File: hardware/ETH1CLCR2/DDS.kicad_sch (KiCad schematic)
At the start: 105 parts, among them Q1201 FDV301N, Q1202 2SC3326B, Q1203 DTA144E, Q1204 DTC114E, U1201 LMH6639MA, U1202 AD9834, U1203 AD8038ARZ, U1204 DAC7811, U1205 AD8038ARZ, U1206 DG409DY, U1207 LMH6639MA, U1208 TL431DBZ, U1209 SN74LVC1T45DBV, U1210 SN74LVC1T45DBV, U1211 74AHC1G14, U1212 SN74LVC1T45DBV, U1213 74AUP1G79, U1214 74AC161, U1215 74AC161, U1216 SN74LVC1T45DBV, X1201 830208220601

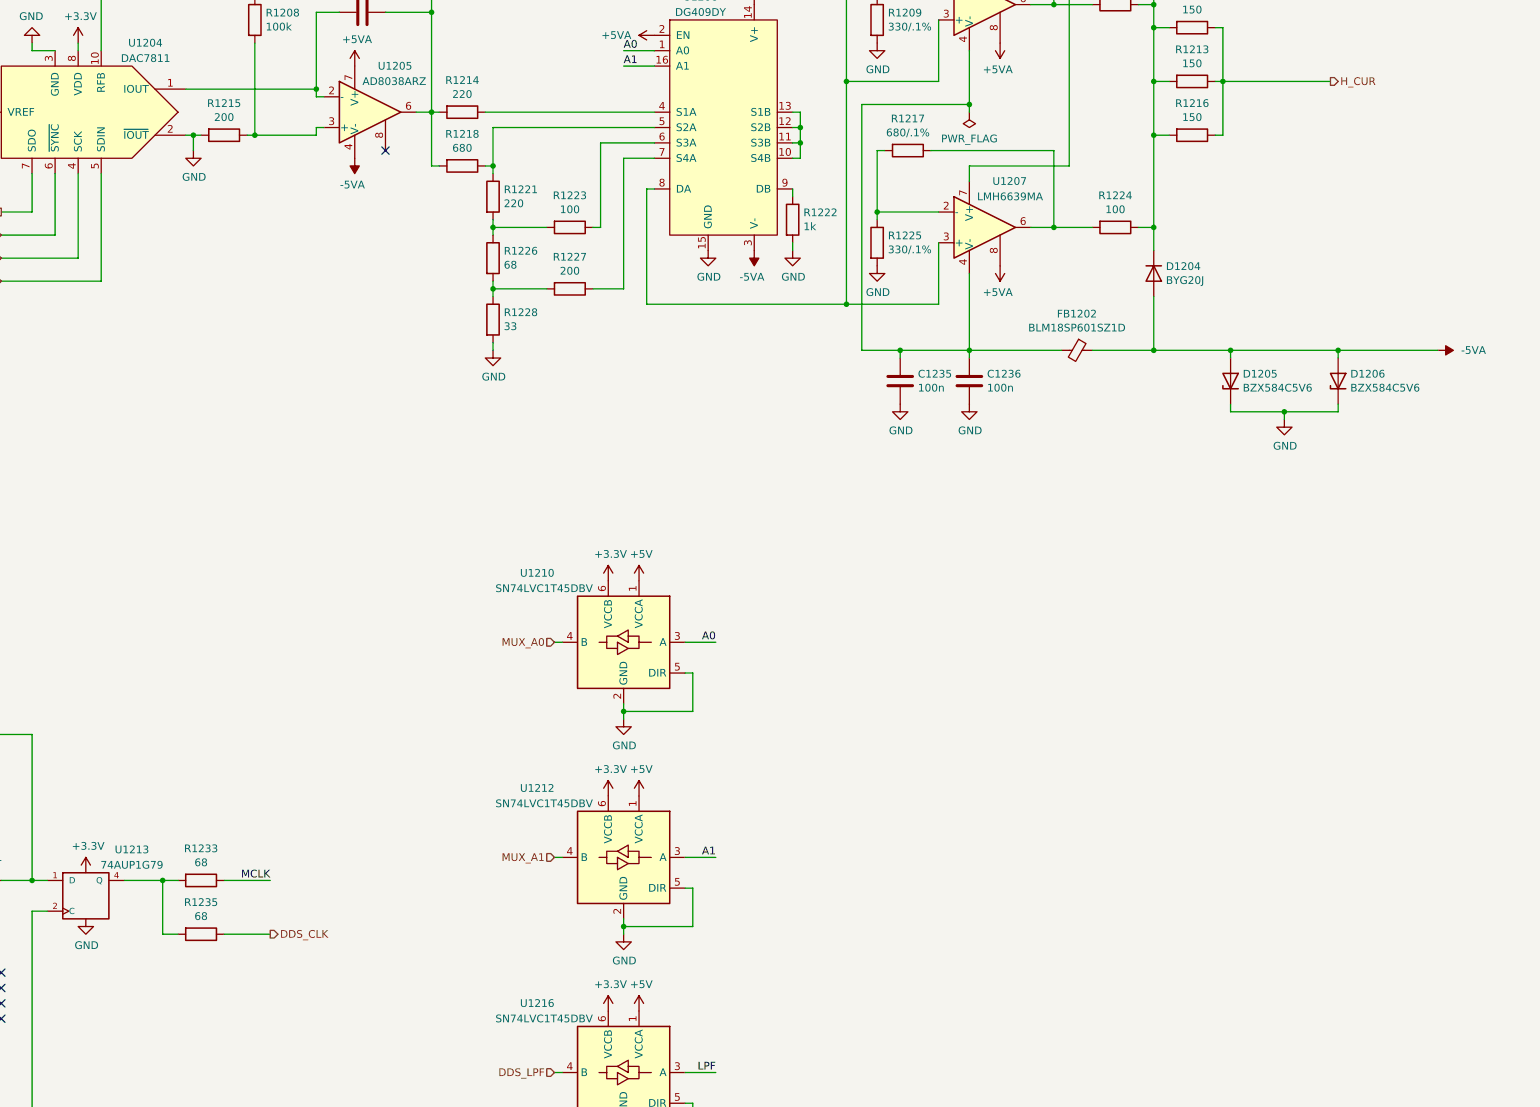
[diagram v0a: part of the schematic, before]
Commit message: Added text to schematics, software development.
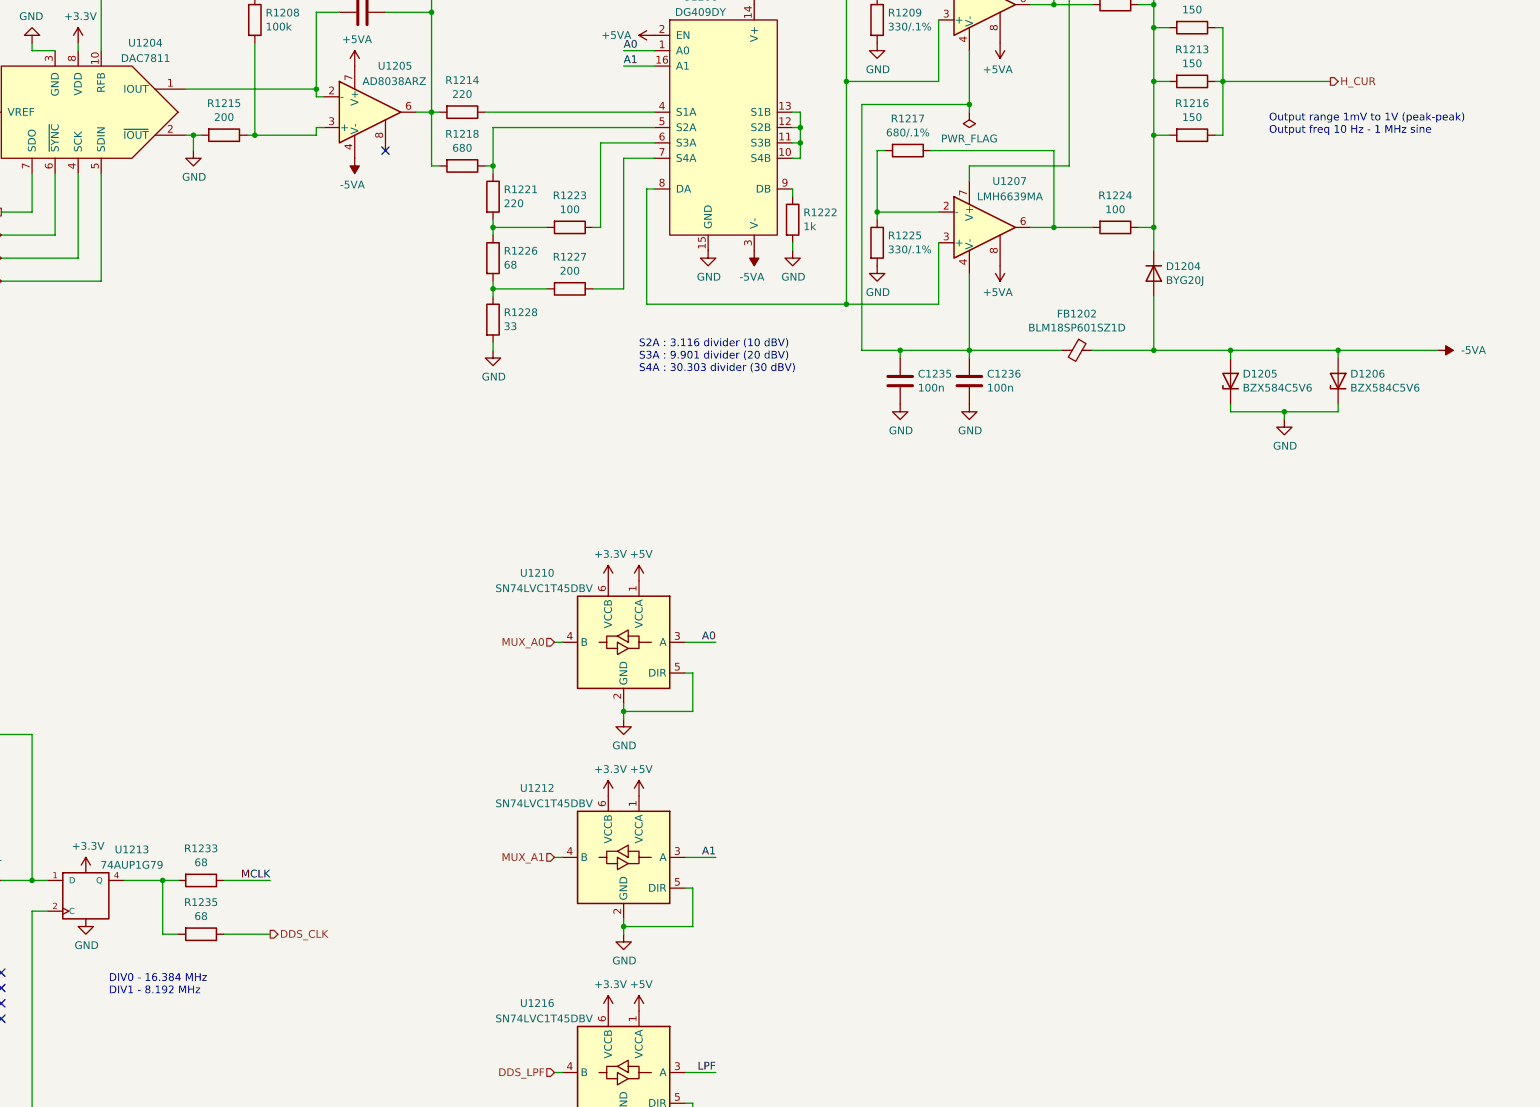
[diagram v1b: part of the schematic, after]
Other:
- note added: "DIV0 - 16.384 MHz DIV1 - 8.192 MHz"
- note added: "Output range 1mV to 1V (peak-peak) Output freq 10 Hz - 1 MHz sine"
- note added: "S2A : 3.116 divider (10 dBV) S3A : 9.901 divider (20 dBV) S4A : 30.303 divider (30 dBV)"
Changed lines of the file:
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@@
     (stroke (width 0) (type default) (color 0 0 0 0))
+  )
+  (text "Output range 1mV to 1V (peak-peak)\nOutput freq 10 Hz - 1 MHz sine"
+    (at 365.76 76.2 0)
+    (effects (font (size 1.27 1.27)) (justify left bottom))
+  )
+  (text "S2A : 3.116 divider (10 dBV)\nS3A : 9.901 divider (20 dBV)\nS4A : 30.303 divider (30 dBV)"
+    (at 261.62 115.57 0)
+    (effects (font (size 1.27 1.27)) (justify left bottom))
+  )
+  (text "DIV0 - 16.384 MHz\nDIV1 - 8.192 MHz" (at 173.99 218.44 0)
+    (effects (font (size 1.27 1.27)) (justify left bottom))
   )
   (label "A0" (at 259.08 62.23 0)

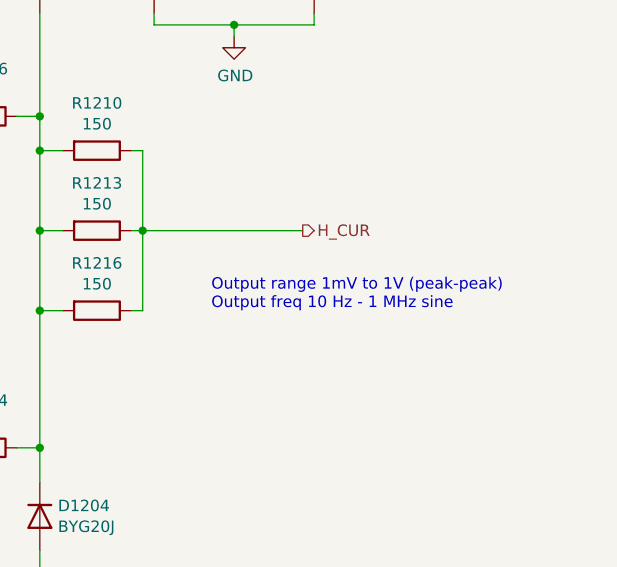
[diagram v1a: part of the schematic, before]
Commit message: Software development and added comments to the schematics.
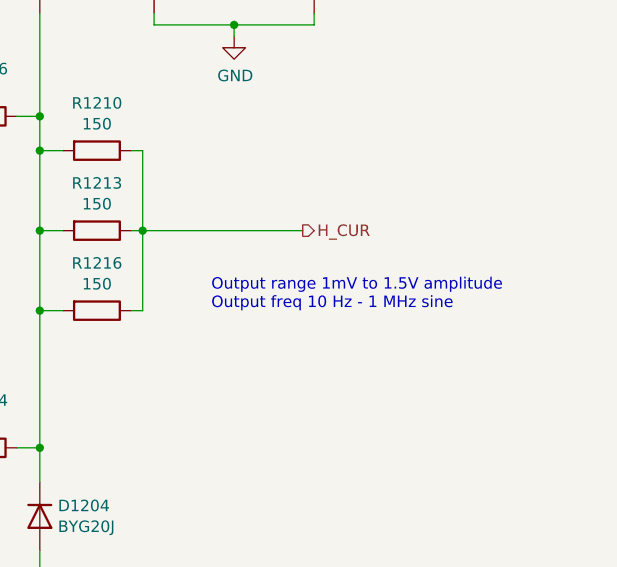
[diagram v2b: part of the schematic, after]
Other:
- note added: "Output range 1mV to 1.5V amplitude Output freq 10 Hz - 1 MHz sine"
- note removed: "Output range 1mV to 1V (peak-peak) Output freq 10 Hz - 1 MHz sine"
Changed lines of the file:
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@@
     (stroke (width 0) (type default) (color 0 0 0 0))
   )
-  (text "Output range 1mV to 1V (peak-peak)\nOutput freq 10 Hz - 1 MHz sine"
+  (text "Output range 1mV to 1.5V amplitude\nOutput freq 10 Hz - 1 MHz sine"
     (at 365.76 76.2 0)
     (effects (font (size 1.27 1.27)) (justify left bottom))

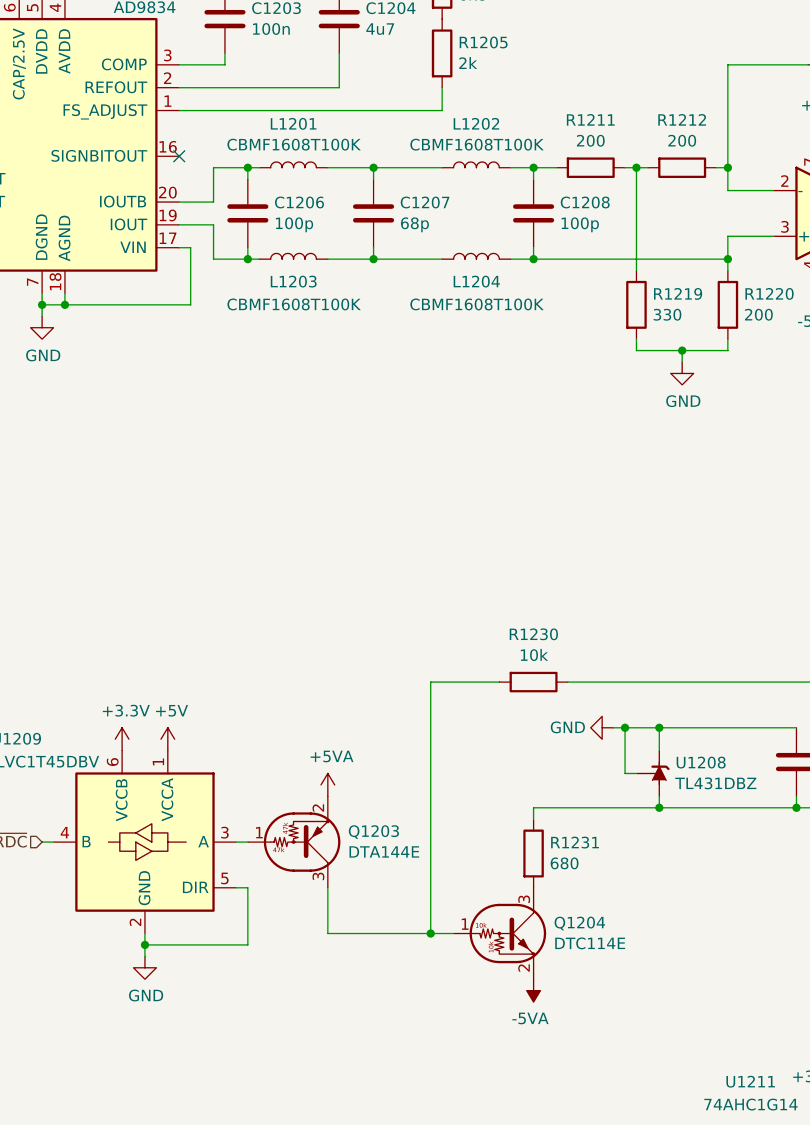
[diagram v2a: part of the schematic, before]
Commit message: Converted HW files to KiCAD 7.0.
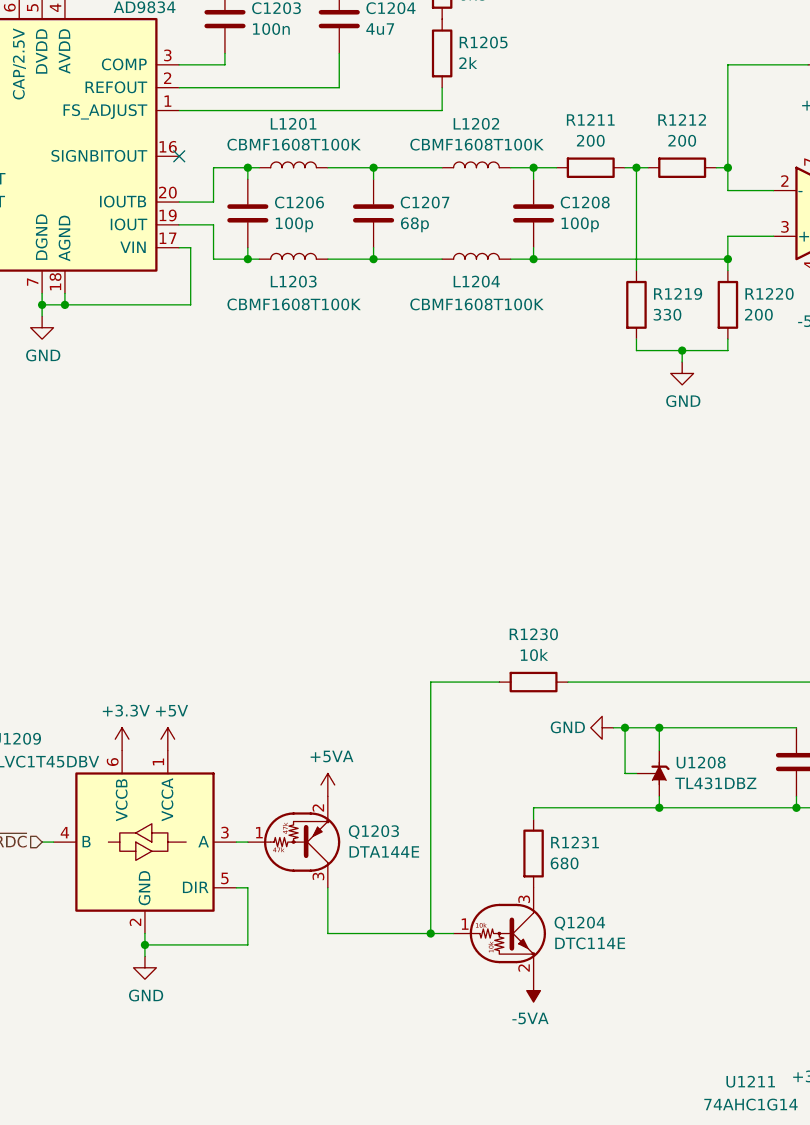
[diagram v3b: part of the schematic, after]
